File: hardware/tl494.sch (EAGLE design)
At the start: 79 parts, among them IC1 TL494CN, J1 CON_HEADER_1X02-PTH, K2 24V, Q1 2N5551, Q1I 8050, Q1I1 2N3904, Q2 8550, Q2I 8050, Q3 8050, Q4 2SK4145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

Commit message: minor updates on board
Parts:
- added H1, H2, H3, H4: MOUNT-PAD-ROUND3.3, holes:MOUNT-PAD-ROUND3.3
- added T2, T4: PAD_TERMINAL-1.02MM_ROUND, dp_devices.v6:PAD_TERMINAL-1.02MM_ROUND
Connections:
- net GND: now also T4.P
- net VOUT: now also T2.P
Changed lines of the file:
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@@
 <?xml version="1.0" encoding="utf-8"?>
 <!DOCTYPE eagle SYSTEM "eagle.dtd">
-<eagle version="9.4.2">
+<eagle version="9.1.3">
 <drawing>
 <settings>
@@
 <part name="GND23" library="dp_devices.v6" deviceset="SUPPLY_GND" device=""/>
 <part name="T3" library="dp_devices.v6" deviceset="PAD_TERMINAL" device="-1.02MM_SQUARE"/>
+<part name="H1" library="holes" library_urn="urn:adsk.eagle:library:237" deviceset="MOUNT-PAD-ROUND" device="3.3" package3d_urn="urn:adsk.eagle:package:14283/1"/>
+<part name="H2" library="holes" library_urn="urn:adsk.eagle:library:237" deviceset="MOUNT-PAD-ROUND" device="3.3" package3d_urn="urn:adsk.eagle:package:14283/1"/>
+<part name="H3" library="holes" library_urn="urn:adsk.eagle:library:237" deviceset="MOUNT-PAD-ROUND" device="3.3" package3d_urn="urn:adsk.eagle:package:14283/1"/>
+<part name="H4" library="holes" library_urn="urn:adsk.eagle:library:237" deviceset="MOUNT-PAD-ROUND" device="3.3" package3d_urn="urn:adsk.eagle:package:14283/1"/>
+<part name="T2" library="dp_devices.v6" deviceset="PAD_TERMINAL" device="-1.02MM_ROUND"/>
+<part name="T4" library="dp_devices.v6" deviceset="PAD_TERMINAL" device="-1.02MM_ROUND"/>
+<part name="GND24" library="dp_devices.v6" deviceset="SUPPLY_GND" device=""/>
 </parts>
 <sheets>
@@
 <attribute name="NAME" x="292.735" y="238.76" size="1.778" layer="95" font="vector" ratio="12" rot="R270"/>
 </instance>
+<instance part="H1" gate="G$1" x="281.94" y="162.56"/>
+<instance part="H2" gate="G$1" x="289.56" y="162.56"/>
+<instance part="H3" gate="G$1" x="297.18" y="162.56"/>
+<instance part="H4" gate="G$1" x="304.8" y="162.56"/>
+<instance part="T2" gate="T" x="345.44" y="50.8" smashed="yes" rot="R270">
+<attribute name="NAME" x="346.075" y="53.34" size="1.778" layer="95" font="vector" ratio="12" rot="R270"/>
+</instance>
+<instance part="T4" gate="T" x="345.44" y="40.64" smashed="yes" rot="R270">
+<attribute name="NAME" x="346.075" y="43.18" size="1.778" layer="95" font="vector" ratio="12" rot="R270"/>
+</instance>
+<instance part="GND24" gate="G$1" x="340.36" y="35.56" smashed="yes"/>
 </instances>
 <busses>
@@
 <wire x1="287.02" y1="236.22" x2="287.02" y2="233.68" width="0.1524" layer="91"/>
 <pinref part="T3" gate="T" pin="P"/>
+</segment>
+<segment>
+<pinref part="T4" gate="T" pin="P"/>
+<pinref part="GND24" gate="G$1" pin="GND"/>
+<wire x1="342.9" y1="40.64" x2="340.36" y2="40.64" width="0.1524" layer="91"/>
+<wire x1="340.36" y1="40.64" x2="340.36" y2="38.1" width="0.1524" layer="91"/>
 </segment>
 </net>
@@
 <pinref part="R3" gate="G$1" pin="2"/>
 <junction x="276.86" y="50.8"/>
-</segment>
-<segment>
+<pinref part="T2" gate="T" pin="P"/>
+<wire x1="342.9" y1="50.8" x2="332.74" y2="50.8" width="0.1524" layer="91"/>
+</segment>
+<segment>

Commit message: fix spice latch circuit, started routing
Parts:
- removed R22: 1K, rcl:R-EU_0207/10
- added J2: CON_HEADER_1X02-PTH, dp_devices.v6:CON_HEADER_1X02-PTH
- C10, C11: value 1000uF 50V -> 1000uF 63V
- R20: value 1K -> 10K
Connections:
- new net N$29: J2.1, OK1.COL
- net GND: no longer OK1.C
- net N$20: now also OK1.A, R20.2; no longer Q1I1.B, R20.1
- net N$33: now also Q1I1.B; no longer R20.2, R22.2
- net N$34: now also OK1.C
- net N$35: now also J2.2, OK1.EMIT; no longer OK1.A, R22.1
- net VIN: now also R20.1
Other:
- note added: "14V out"
- note added: "18 turns on black ferrite ring"
- note added: "48V Input"
- note added: "Input Vf = 1.2V"
- note added: "SW"
- note added: "To Arduino wake-up SW"
- note removed: "18 turns on black ferrite core ring"
- note removed: "Initial SW"
- moved on the sheet: C3, D1, OK1, R12, R20, RT1, T1, T3

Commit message: done board routing
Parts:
- removed H3, H4: MOUNT-PAD-ROUND3.3, holes:MOUNT-PAD-ROUND3.3
- removed L1: INDUCTOR-L1812, dp_devices.v6:INDUCTOR-L1812
- added J3: J20MM, jumper:J20MM
- added J4: J5MM, jumper:J5MM
- added J5: J15MM, jumper:J15MM
- added L2: (no value), rcl:L-EUTJ5-U1
- added R22: 560R 1W, trosh_devices.eagle.v9:RESISTOR0414V_EXPAD
- C1, C13, C14, C15, C2, C3, C4, C5, C6, C8, C9: device rcl:C-EU050-024X044 -> trosh_devices.eagle.v9:CAPACITORC050-024X044_EXPAD
- C16: device rcl:CPOL-EUE2.5-7 -> trosh_devices.eagle.v9:CAPACITOR-POLE2,5-7_EXPAD
- C17: device rcl:CPOL-EUE2-5 -> trosh_devices.eagle.v9:CAPACITOR-POLE2,5_EXPAD
- C7: device rcl:C-EU050-050X075 -> trosh_devices.eagle.v9:CAPACITORC050-050X075_EXPAD
- R1, R10, R11, R12, R15, R16, R2, R20, R25, R27, R28, R29, R3, R30, R31, R6, R7, R8, R9: device rcl:R-EU_0207/10 -> trosh_devices.eagle.v9:RESISTOR-0207/10_EXPAD
- R13: device rcl:R-EU_0207/2V -> trosh_devices.eagle.v9:RESISTOR0207/2V_EXPAD
- R14, R17, R21, R32, R34, R35, R4, R5: device rcl:R-EU_0207/10 -> trosh_devices.eagle.v9:RESISTOR0207/2V_EXPAD
- R18, R19: device rcl:R-EU_0207/10 -> trosh_devices.eagle.v9:RESISTOR0414V_EXPAD
- R26: value 560*x2 1W -> 560R 1W; device rcl:R-EU_0207/10 -> trosh_devices.eagle.v9:RESISTOR0414V_EXPAD
- R33: device rcl:R-EU_0414/5V -> trosh_devices.eagle.v9:RESISTOR0414V_EXPAD
- R36: device rcl:R-EU_0207/10 -> rcl:R-EU_0207/2V
- RT1: value (none) -> RESISTOR0207/2V_EXPAD; device rcl:R-EU_0207/2V -> trosh_devices.eagle.v9:RESISTOR0207/2V_EXPAD
- R_ADJ: device dp_devices.v6:TRIMMER-3362P -> trosh_devices.eagle.v9:TRIMMER-3362P_EXPAD
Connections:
- new net N$36: R22.2, R26.1
- new net N$37: D3.C, J3.2, L2.2
- new net N$38: J3.1, J4.1, Q4.S
- net +15V: now also R33.2; no longer R33.1
- net +V: now also R33.1; no longer R33.2
- net GND: now also J5.1, J5.2
- net N$17: now also J4.2; no longer D3.C, L1.1, Q4.S
- net N$18: now also R18.2; no longer R18.1
- net N$19: now also R18.1; no longer R18.2
- net N$22: now also R26.2; no longer R26.1
- net N$32: now also R22.1; no longer R26.2
- net VOUT: now also L2.1; no longer L1.2
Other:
- note added: "replace this with smaller P-MOSFET"

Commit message: place values
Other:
- note added: "108 Khz 3.2Vp-p"
- note added: "17mA"
- note added: "48V Input MOD circuit"
- note added: "VGS 2.62V"
- note added: "Vr=17.44V"
- note added: "Vr=31.19V"
- note added: "this needs a pass transistor regulator"
- note removed: "~60V Input MOD circuit"
- moved on the sheet: C7, R18
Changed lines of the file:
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@@
 <wire x1="127" y1="71.12" x2="83.82" y2="71.12" width="0.1524" layer="98" style="shortdash"/>
 <wire x1="83.82" y1="71.12" x2="83.82" y2="124.46" width="0.1524" layer="98" style="shortdash"/>
-<text x="104.14" y="73.66" size="1.778" layer="98" align="center">~60V Input MOD circuit</text>
+<text x="104.14" y="73.66" size="1.778" layer="98" align="center">48V Input MOD circuit</text>
 <text x="-2.54" y="-27.94" size="1.778" layer="98">91.65 Khz 3.2Vp-p</text>
 <text x="0" y="17.78" size="1.778" layer="98">2.02V</text>
@@
 <text x="350.52" y="45.72" size="1.778" layer="98">14V out</text>
 <text x="215.9" y="248.92" size="1.778" layer="98">replace this with smaller P-MOSFET</text>
+<text x="106.68" y="106.68" size="1.778" layer="98" align="center">17mA</text>
+<text x="116.84" y="109.22" size="1.778" layer="98" align="center">this needs a
+pass transistor
+regulator</text>
+<text x="-2.54" y="-30.48" size="1.778" layer="98">108 Khz 3.2Vp-p</text>
+<text x="187.96" y="55.88" size="1.778" layer="98">VGS 2.62V</text>
+<text x="93.98" y="12.7" size="1.778" layer="98">Vr=17.44V</text>
+<text x="167.64" y="30.48" size="1.778" layer="98">Vr=31.19V</text>
 </plain>
 <instances>
@@
 <attribute name="VALUE" x="180.34" y="25.4" size="1.778" layer="96"/>
 </instance>
-<instance part="R18" gate="R" x="165.1" y="33.02" smashed="yes" rot="R270">
-<attribute name="NAME" x="163.83" y="31.5214" size="1.778" layer="95" rot="R180"/>
-<attribute name="VALUE" x="163.83" y="33.782" size="1.778" layer="96" rot="R180"/>
-</instance>
-<instance part="C7" gate="G$1" x="180.34" y="40.64" smashed="yes" rot="R90">
-<attribute name="NAME" x="182.88" y="45.72" size="1.778" layer="95" rot="R180"/>
-<attribute name="VALUE" x="182.88" y="48.26" size="1.778" layer="96" rot="R180"/>
+<instance part="R18" gate="R" x="165.1" y="30.48" smashed="yes" rot="R270">
+<attribute name="NAME" x="163.83" y="28.9814" size="1.778" layer="95" rot="R180"/>
+<attribute name="VALUE" x="163.83" y="31.242" size="1.778" layer="96" rot="R180"/>
+</instance>
+<instance part="C7" gate="G$1" x="180.34" y="38.1" smashed="yes" rot="R90">
+<attribute name="NAME" x="182.88" y="43.18" size="1.778" layer="95" rot="R180"/>
+<attribute name="VALUE" x="182.88" y="45.72" size="1.778" layer="96" rot="R180"/>
 </instance>
 <instance part="D5" gate="1" x="165.1" y="43.18" smashed="yes" rot="R270">
-<attribute name="NAME" x="167.64" y="43.6626" size="1.778" layer="95"/>
-<attribute name="VALUE" x="167.64" y="40.8686" size="1.778" layer="96"/>
+<attribute name="NAME" x="154.94" y="43.6626" size="1.778" layer="95"/>
+<attribute name="VALUE" x="154.94" y="40.8686" size="1.778" layer="96"/>
 </instance>
 <instance part="C8" gate="G$1" x="175.26" y="12.7" smashed="yes">
@@
 <wire x1="165.1" y1="22.86" x2="109.22" y2="22.86" width="0.1524" layer="91"/>
 <wire x1="109.22" y1="22.86" x2="109.22" y2="17.78" width="0.1524" layer="91"/>
-<wire x1="165.1" y1="27.94" x2="165.1" y2="22.86" width="0.1524" layer="91"/>
+<wire x1="165.1" y1="25.4" x2="165.1" y2="22.86" width="0.1524" layer="91"/>
 <wire x1="175.26" y1="15.24" x2="175.26" y2="22.86" width="0.1524" layer="91"/>
 <junction x="175.26" y="22.86"/>
@@
 <pinref part="C7" gate="G$1" pin="1"/>
 <pinref part="D5" gate="1" pin="C"/>
-<wire x1="165.1" y1="40.64" x2="177.8" y2="40.64" width="0.1524" layer="91"/>
 <wire x1="165.1" y1="40.64" x2="165.1" y2="38.1" width="0.1524" layer="91"/>
-<junction x="165.1" y="40.64"/>
+<wire x1="165.1" y1="38.1" x2="165.1" y2="35.56" width="0.1524" layer="91"/>
+<wire x1="177.8" y1="38.1" x2="165.1" y2="38.1" width="0.1524" layer="91"/>
+<junction x="165.1" y="38.1"/>
 </segment>
 </net>
@@
 <segment>
 <pinref part="C7" gate="G$1" pin="2"/>
-<wire x1="185.42" y1="40.64" x2="193.04" y2="40.64" width="0.1524" layer="91"/>
-<wire x1="193.04" y1="40.64" x2="193.04" y2="38.1" width="0.1524" layer="91"/>
+<wire x1="185.42" y1="38.1" x2="198.12" y2="38.1" width="0.1524" layer="91"/>
 <pinref part="J4" gate="1" pin="2"/>
-<wire x1="193.04" y1="38.1" x2="198.12" y2="38.1" width="0.1524" layer="91"/>
 <pinref part="Q2" gate="Q" pin="C"/>
 <wire x1="165.1" y1="-10.16" x2="165.1" y2="-12.7" width="0.1524" layer="91"/>

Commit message: updated the board
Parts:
- added H3, H4, H5: HEATSINK1, trosh_devices.eagle.v9:HEATSINK1
- added Q5: TIP31, trosh_devices.eagle.v9:Q_NPN_TIP31
- D10: value 15V 1/2W -> 16V 1/4W
- D2: device diode:1N4933 -> trosh_devices.eagle.v9:DIODEDO41-2.5V
- D4: device diode:1N4148DO35-10 -> trosh_devices.eagle.v9:DIODEDO35-20
- R15, R30, R31, R7, R8: device trosh_devices.eagle.v9:RESISTOR-0207/10_EXPAD -> trosh_devices.eagle.v9:RESISTOR0207/2V_EXPAD
- R33: value 4K 2W -> 100K; device trosh_devices.eagle.v9:RESISTOR0414V_EXPAD -> trosh_devices.eagle.v9:RESISTOR0207/2V_EXPAD
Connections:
- new net N$39: D10.C, Q5.B, R33.2
- net +15V: now also Q5.E; no longer D10.C, R33.2
- net +V: now also Q5.C
- net N$16: now also R17.2; no longer R17.1
- net N$17: now also R17.1; no longer R17.2
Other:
- note removed: "this needs a pass transistor regulator"
- moved on the sheet: C16, D10, R17, R33

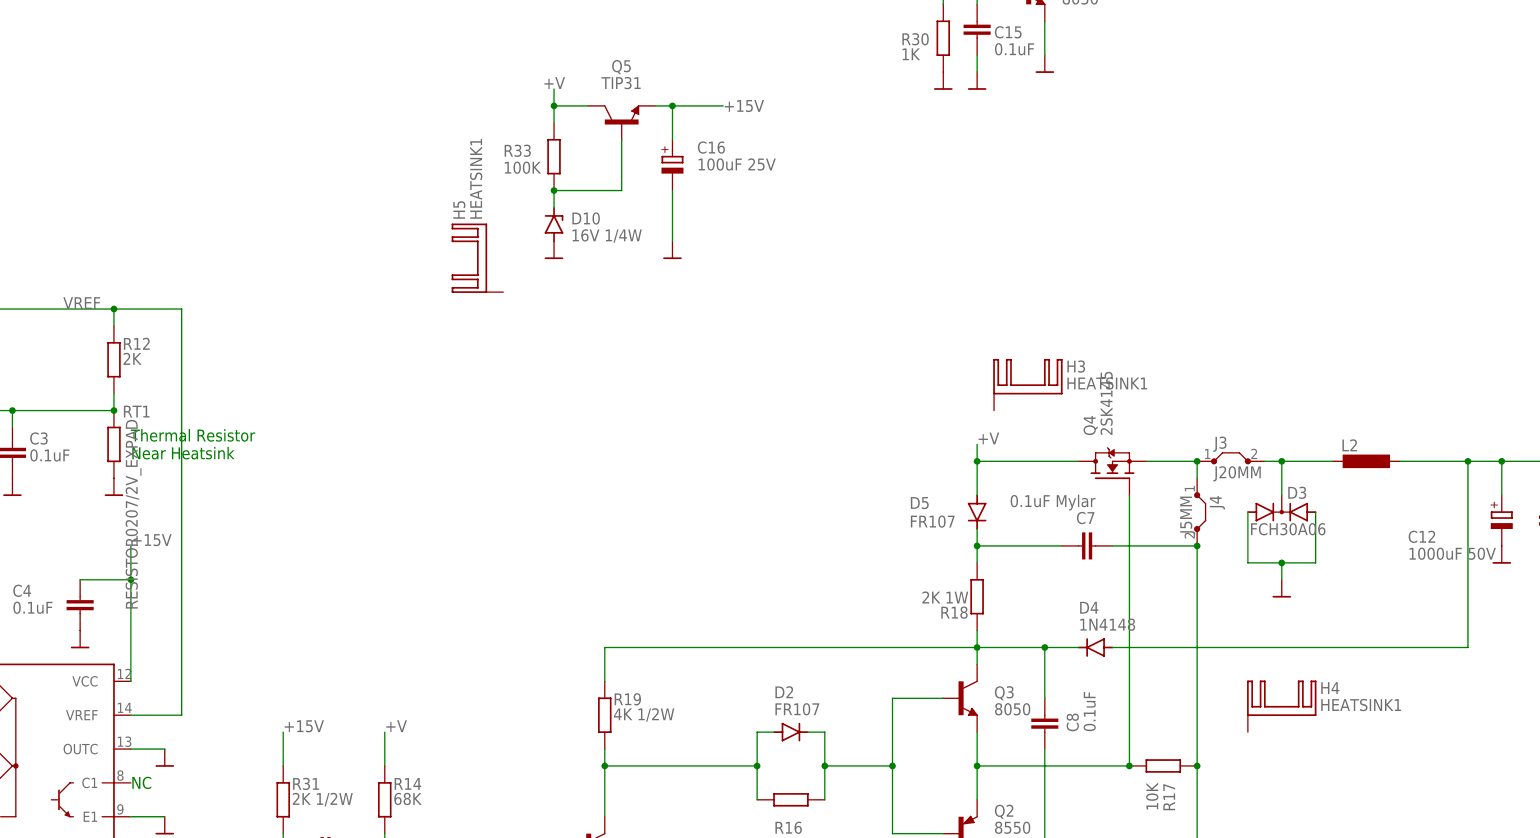
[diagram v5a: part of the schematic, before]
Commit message: added measured values on schematic
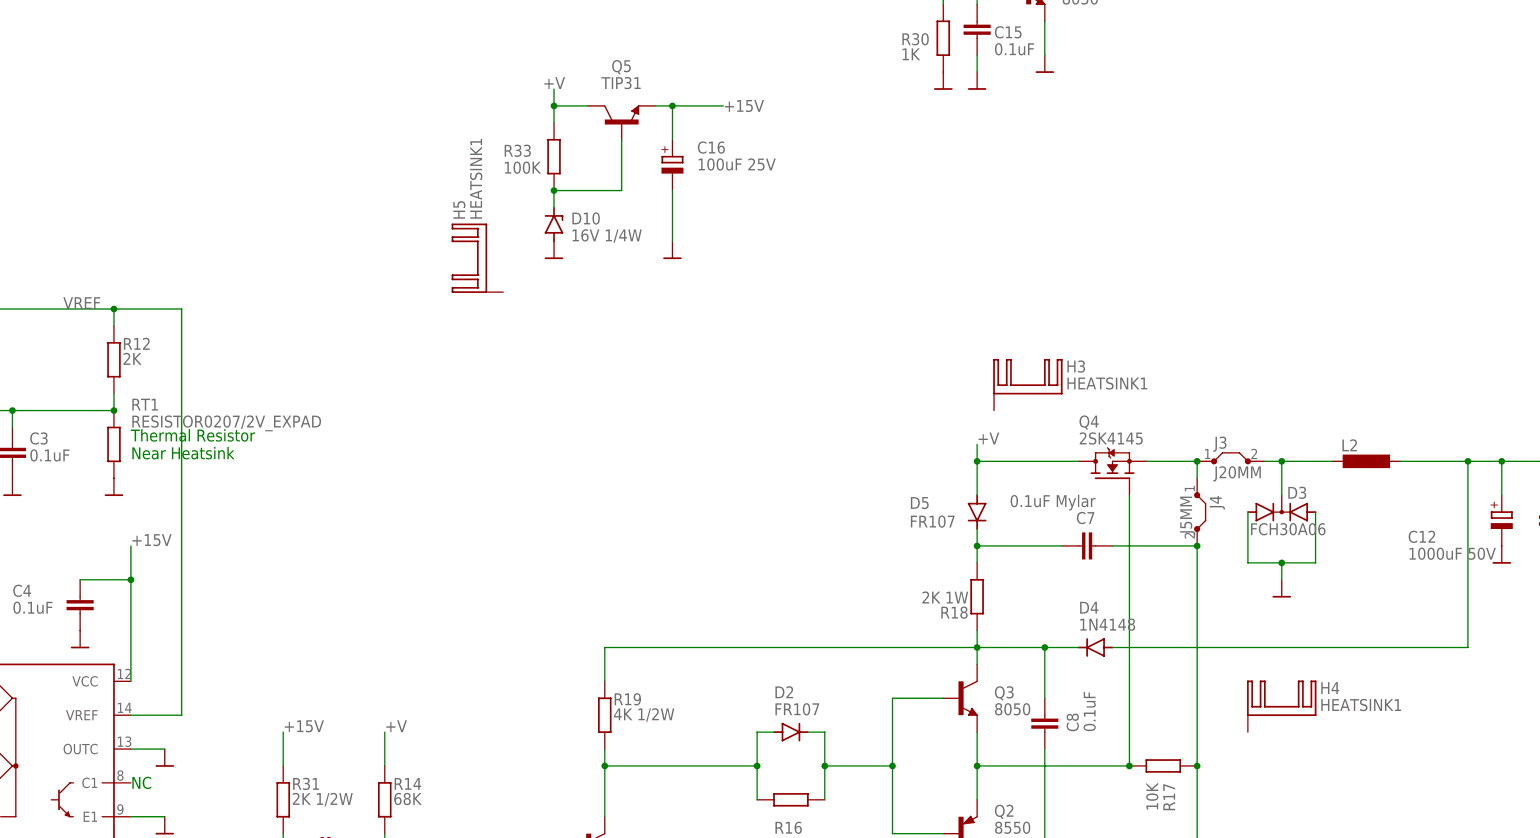
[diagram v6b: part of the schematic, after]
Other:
- note added: "17mA diode current"
- note added: "18 turns Ferrite Ring Black OD - 17.5mm ID - 9.5mm Thickness - 7mm"
- note added: "350R Room Temp"
- note added: "Ir=12mA (working)"
- note added: "Ir=17mA"
- note added: "Ir=9mA(not working)"
- note removed: "18 turns on black ferrite ring"
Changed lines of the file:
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@@
 <?xml version="1.0" encoding="utf-8"?>
 <!DOCTYPE eagle SYSTEM "eagle.dtd">
-<eagle version="9.1.3">
+<eagle version="9.4.2">
 <drawing>
 <settings>
@@
 <text x="71.12" y="157.48" size="1.778" layer="98">Original C11 is 1000uF 50V
 to 1000uF 63V</text>
-<text x="215.9" y="55.88" size="1.778" layer="98">18 turns on black ferrite ring</text>
+<text x="215.9" y="55.88" size="1.778" layer="98">18 turns
+Ferrite Ring Black
+OD - 17.5mm
+ID - 9.5mm
+Thickness - 7mm</text>
 <text x="210.82" y="236.22" size="1.778" layer="98">SW</text>
 <text x="241.3" y="208.28" size="1.778" layer="98">Latch circuit</text>
@@
 <text x="106.68" y="96.52" size="1.778" layer="98" align="center">17mA</text>
 <text x="-2.54" y="-30.48" size="1.778" layer="98">108 Khz 3.2Vp-p</text>
-<text x="187.96" y="55.88" size="1.778" layer="98">VGS 2.62V</text>
-<text x="93.98" y="12.7" size="1.778" layer="98">Vr=17.44V</text>
+<text x="190.5" y="55.88" size="1.778" layer="98">VGS 2.62V</text>
+<text x="93.98" y="15.24" size="1.778" layer="98">Vr=17.44V</text>
 <text x="167.64" y="30.48" size="1.778" layer="98">Vr=31.19V</text>
+<text x="38.1" y="48.26" size="1.778" layer="98">350R Room Temp</text>
+<text x="210.82" y="165.1" size="1.778" layer="98">17mA diode current</text>
+<text x="86.36" y="12.7" size="1.778" layer="98">Ir=12mA (working)</text>
+<text x="86.36" y="10.16" size="1.778" layer="98">Ir=9mA(not working)</text>
+<text x="167.64" y="33.02" size="1.778" layer="98">Ir=17mA</text>
 </plain>
 <instances>
@@
 <instance part="GND6" gate="G$1" x="20.32" y="45.72" smashed="yes"/>
 <instance part="RT1" gate="R" x="35.56" y="53.34" smashed="yes" rot="R270">
-<attribute name="NAME" x="36.83" y="57.3786" size="1.778" layer="95"/>
-<attribute name="VALUE" x="37.338" y="57.15" size="1.778" layer="96" rot="R270"/>
+<attribute name="NAME" x="38.1" y="58.42" size="1.778" layer="95"/>
+<attribute name="VALUE" x="38.1" y="55.88" size="1.778" layer="96"/>
 </instance>
 <instance part="GND7" gate="G$1" x="35.56" y="45.72" smashed="yes"/>
@@
 </instance>
 <instance part="Q4" gate="Q" x="185.42" y="48.26" smashed="yes" rot="R90">
-<attribute name="VALUE" x="185.42" y="54.61" size="1.778" layer="96" rot="R90"/>
-<attribute name="NAME" x="182.88" y="54.61" size="1.778" layer="95" rot="R90"/>
+<attribute name="VALUE" x="180.34" y="53.34" size="1.778" layer="96"/>
+<attribute name="NAME" x="180.34" y="55.88" size="1.778" layer="95"/>
 </instance>
 <instance part="D3" gate="-B1" x="210.82" y="43.18" smashed="yes">
@@
 <attribute name="VALUE" x="219.71" y="47.498" size="1.778" layer="96"/>
 </instance>
-<instance part="H3" gate="G$1" x="172.72" y="60.96"/>
-<instance part="H4" gate="G$1" x="210.82" y="12.7"/>
-<instance part="H5" gate="G$1" x="91.44" y="81.28" rot="R90"/>
+<instance part="H3" gate="G$1" x="172.72" y="60.96" smashed="yes">
+<attribute name="NAME" x="178.435" y="64.135" size="1.778" layer="95"/>
+<attribute name="VALUE" x="178.435" y="61.595" size="1.778" layer="96"/>
+</instance>
+<instance part="H4" gate="G$1" x="210.82" y="12.7" smashed="yes">
+<attribute name="NAME" x="216.535" y="15.875" size="1.778" layer="95"/>
+<attribute name="VALUE" x="216.535" y="13.335" size="1.778" layer="96"/>
+</instance>
+<instance part="H5" gate="G$1" x="91.44" y="81.28" smashed="yes" rot="R90">
+<attribute name="NAME" x="88.265" y="86.995" size="1.778" layer="95" rot="R90"/>
+<attribute name="VALUE" x="90.805" y="86.995" size="1.778" layer="96" rot="R90"/>
+</instance>
 <instance part="Q5" gate="G$1" x="111.76" y="101.6" smashed="yes" rot="R90">
 <attribute name="NAME" x="111.76" y="109.22" size="1.778" layer="95" align="bottom-center"/>

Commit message: added micro-cap spice sim
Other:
- note added: "Ib=188uA"
- note added: "Ic=15.1mA"
- note added: "Vdivider, V@R15 @Vin 24V = 1.552V @Vin 48V = 3.103V orig values R14 = 68K, R15 = 4.7K, I=330uA new values R14=130k, R15=4.3k, I=357uA"
- note added: "Vr=15.66V"
- note added: "Vr=7.08V"
- note added: "~48V"
- moved on the sheet: C12, C13, D3, D4, H4, J3, J4, L2, LED1, Q4, R1, R10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

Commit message: schematic tiny updates
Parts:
- R14: value 68K -> 130K
- R15: value 4.7K -> 4.3K
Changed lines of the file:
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@@
 <?xml version="1.0" encoding="utf-8"?>
 <!DOCTYPE eagle SYSTEM "eagle.dtd">
-<eagle version="9.1.3">
+<eagle version="9.4.2">
 <drawing>
 <settings>
@@
 <part name="R13" library="trosh_devices.eagle.v9" deviceset="RESISTOR" device="0207/2V_EXPAD" value="10K"/>
 <part name="C6" library="trosh_devices.eagle.v9" deviceset="CAPACITOR" device="C050-024X044_EXPAD" value="0.1uF"/>
-<part name="R14" library="trosh_devices.eagle.v9" deviceset="RESISTOR" device="0207/2V_EXPAD" value="68K"/>
-<part name="R15" library="trosh_devices.eagle.v9" deviceset="RESISTOR" device="0207/2V_EXPAD" value="4.7K"/>
+<part name="R14" library="trosh_devices.eagle.v9" deviceset="RESISTOR" device="0207/2V_EXPAD" value="130K"/>
+<part name="R15" library="trosh_devices.eagle.v9" deviceset="RESISTOR" device="0207/2V_EXPAD" value="4.3K"/>
 <part name="GND14" library="dp_devices.v6" deviceset="SUPPLY_GND" device=""/>
 <part name="Q1" library="dp_devices.v6" deviceset="TRANSISTOR_BJT_NPN" device="-TO-92-EBC" value="2N5551"/>
